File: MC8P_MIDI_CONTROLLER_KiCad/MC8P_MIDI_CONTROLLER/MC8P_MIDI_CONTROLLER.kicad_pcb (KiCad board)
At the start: 2 copper layers, 310.5 x 184.5 mm, 51 parts, among them J1 MIDI OUT, SW1 ASSIGN, SW2 ENTER, SW3 PREV, SW4 NEXT, U1 Teensy4.0

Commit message: V1.0.2
- KiCad Modifications
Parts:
- removed the G*** at (334.1, 61.6)
- added G***: LOGO, AXS_LOGO_KICAD:AXS_LOGO_FMASK_30X30, F.Cu at (224.5, 41.2)
- added G***: LOGO, MC8P_BITMAP_FOOTPRINTS:MC8P_MANUAL_QR_SLKSCR_20X20, F.Cu at (243.0, 39.5)
- added G***: LOGO, AXS_LOGO_KICAD:AXS_LOGO_FMASK_30X30, F.Cu at (78.5, 138.5)
- moved ? 7.00 mm to (324.5, 26.0)
- moved ? 7.00 mm to (324.5, 106.0)
- moved ? 7.00 mm to (181.5, 26.0)
- moved ? 7.00 mm to (169.0, 198.5)
- moved ? 7.00 mm to (181.5, 106.0)
- moved ? 7.00 mm to (26.0, 198.5)
- moved ? 7.00 mm to (26.0, 106.0)
- moved ? 7.00 mm to (169.0, 118.5)
- moved ? 7.00 mm to (26.0, 118.5)
- moved C1 7.00 mm to (76.0, 53.0)
- moved C2 7.00 mm to (81.0, 53.0)
- moved C3 7.00 mm to (86.0, 53.0)
- moved C4 7.00 mm to (91.0, 53.0)
- moved C5 7.00 mm to (111.0, 53.0)
- moved C6 7.00 mm to (106.0, 53.0)
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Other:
- board text added: ".AXS INTRUMENTS"
- board text added: "MAX"
- board text added: "MC8P"
- board text added: "MIN"
- board text added: "STANDALONE MIDI CONTROLLER"
- board text added: "TYPE A"

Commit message: v1.0.3
- Back panel finalised
- Exported gerbers
- Panelised for DIY kits
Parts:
- added G*** (x2): LOGO, MC8P_BITMAP_FOOTPRINTS:MC8P_PXLART_SPACE_FMASK_45X40, F.Cu at (251.9, 132.0)
- added G***: LOGO, MC8P_BITMAP_FOOTPRINTS:MC8P_PXLART_SPACE_FMASK_45X40, F.Cu at (256.2, 122.5)
- moved ? 162.1 mm to (271.0, 179.0), turned to 90 degrees
- moved ? 152.2 mm to (191.0, 179.0), turned to 90 degrees
- moved ? 90.1 mm to (271.0, 36.0), turned to 90 degrees
- moved ? 70.6 mm to (191.0, 36.0), turned to 90 degrees
- moved G*** 59.8 mm to (257.5, 97.5), turned to -90 degrees
- moved G*** 50.5 mm to (255.8, 80.8), turned to -90 degrees
- moved C1 14.1 mm to (86.0, 63.0)
- moved C2 14.1 mm to (91.0, 63.0)
- moved C3 14.1 mm to (96.0, 63.0)
- moved C4 14.1 mm to (101.0, 63.0)
- moved C5 14.1 mm to (121.0, 63.0)
- moved C6 14.1 mm to (116.0, 63.0)
- moved C7 14.1 mm to (111.0, 63.0)
- moved C8 14.1 mm to (106.0, 63.0)
- moved J1 14.1 mm to (48.5, 36.5)
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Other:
- board size 310.5 x 184.5 mm -> 247 x 196 mm
- board text added: ".AXS INSTRUMENTS"
- board text added: ">> NEXT"
- board text added: "I hope this controller becomes a trusted companion in your creative workflow - always ready to shape your sounds and aid in bringing your ideas to life! - Joe <3"
- board text added: "SNo."
- board text added: "THANK YOU"
- board text removed: "NEXT >>"

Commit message: Gerber Edits
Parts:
- moved ? 187.9 mm to (310.2, 181.1), turned to -90 degrees
- moved ? 184.6 mm to (310.2, 38.1), turned to -90 degrees
- moved ? 184.2 mm to (218.2, 181.2), turned to 90 degrees
- moved ? 174.3 mm to (218.2, 38.2), turned to 90 degrees
- moved REF** 160.5 mm to (205.5, 170.2), turned to 90 degrees
- moved ? 150.7 mm to (230.2, 181.1), turned to -90 degrees
- moved ? 146.6 mm to (230.2, 38.1), turned to -90 degrees
- moved REF** 145.5 mm to (46.2, 181.2), turned to 90 degrees
- moved REF** 143.8 mm to (205.5, 147.2), turned to 90 degrees
- moved REF** 134.6 mm to (181.5, 170.2), turned to 90 degrees
- moved REF** 133.1 mm to (205.5, 124.2), turned to 90 degrees
- moved REF** 132.8 mm to (46.2, 38.2), turned to 90 degrees
- moved J1 132.2 mm to (46.7, 168.7), turned to -90 degrees
- moved REF** 129.9 mm to (205.5, 101.2), turned to 90 degrees
- moved R5 124.5 mm to (60.6, 173.7), turned to 180 degrees
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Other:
- board size 247 x 196 mm -> 288 x 155 mm

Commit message: v1.0.4
- Design update with new logo
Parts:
- removed the G*** at (245.4, 136.4)
- removed the G*** at (158.2, 128.6)
- added G***: LOGO, AXS_LOGO_KICAD:AXS_LOGO_FMASK_20X20, F.Cu at (78.5, 136.5)
- added G***: LOGO, AXS_LOGO_KICAD:AXS_LOGO_FMASK_43X43, F.Cu at (97.5, 262.0)
- moved ? 304.4 mm to (26.0, 290.0), turned to 180 degrees
- moved ? 288.8 mm to (169.0, 290.0), turned to 180 degrees
- moved ? 206.3 mm to (26.0, 210.0), turned to 180 degrees
- moved ? 193.0 mm to (26.0, 198.0), turned to 0 degrees
- moved G*** 192.2 mm to (122.0, 229.1), turned to 0 degrees (x2)
- moved G*** 187.6 mm to (87.5, 223.5), turned to 0 degrees
- moved G*** 185.7 mm to (112.5, 224.8), turned to 0 degrees
- moved ? 182.4 mm to (169.0, 210.0), turned to 180 degrees
- moved REF** 169.2 mm to (37.0, 185.2), turned to 0 degrees
- moved ? 167.3 mm to (169.0, 198.0), turned to 0 degrees
- moved REF** 156.5 mm to (26.0, 26.0), turned to 0 degrees
- moved REF** 150.4 mm to (60.0, 185.2), turned to 0 degrees
- moved REF** 144.8 mm to (37.0, 161.3), turned to 0 degrees
- moved J1 142.4 mm to (38.5, 26.5), turned to 180 degrees
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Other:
- board size 288 x 155 mm -> 155 x 288 mm

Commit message: v1.0.6
-Adjustments to Front Panel and button positions
- Beginning Blender Models
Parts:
- moved SW1 1.50 mm to (135.0, 65.9)
- moved SW2 1.50 mm to (155.2, 65.9)
- moved SW3 1.50 mm to (135.0, 85.9)
- moved SW4 1.50 mm to (155.2, 85.9)
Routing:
- net D5: track 274.6 -> 278.5 mm
- net Vcc: track 486.5 -> 489.9 mm
- net D7: track 254.8 -> 257.7 mm
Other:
- outline, holes or cut-outs redrawn

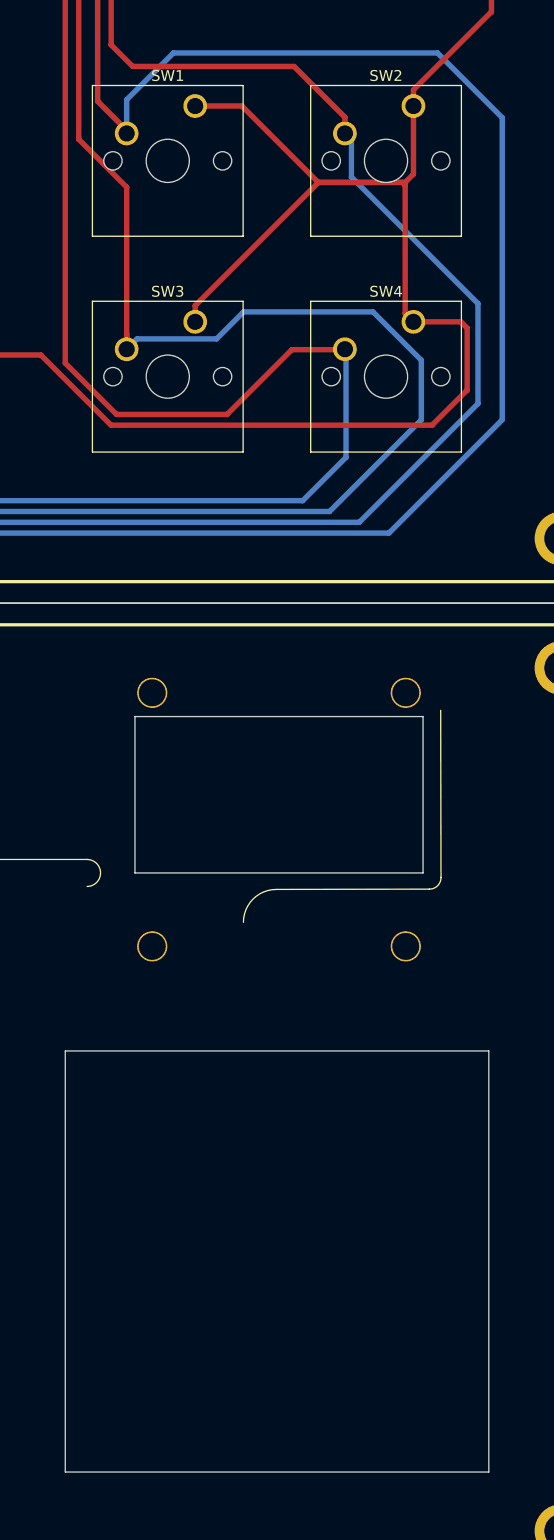
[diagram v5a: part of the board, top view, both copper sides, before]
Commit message: v1.0.9
- Panel alterations
- Sketchup alterations
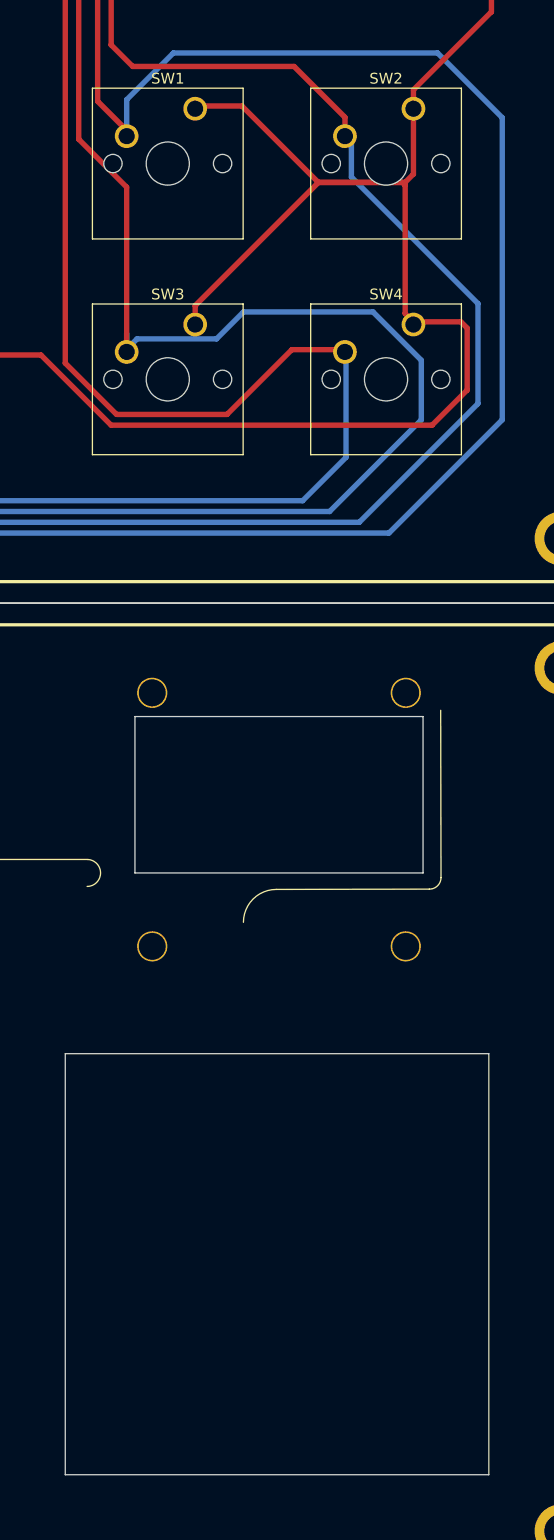
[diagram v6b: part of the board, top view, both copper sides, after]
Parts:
- moved SW1 0.25 mm to (135.0, 66.2)
- moved SW2 0.25 mm to (155.2, 66.2)
- moved SW3 0.25 mm to (135.0, 86.2)
- moved SW4 0.25 mm to (155.2, 86.2)
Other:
- outline, holes or cut-outs redrawn

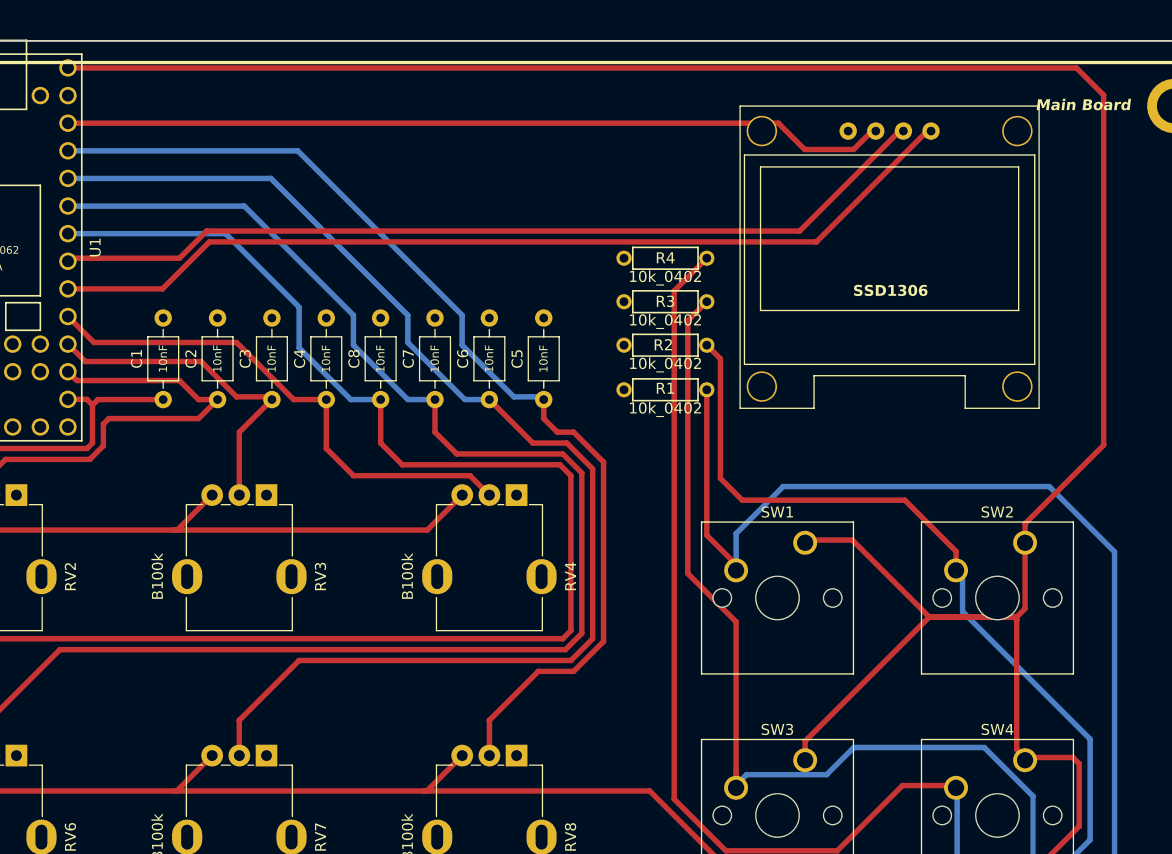
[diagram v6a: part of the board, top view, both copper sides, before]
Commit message: v1.1.0
- PCB Fixes
- firmware descriptor adjustments
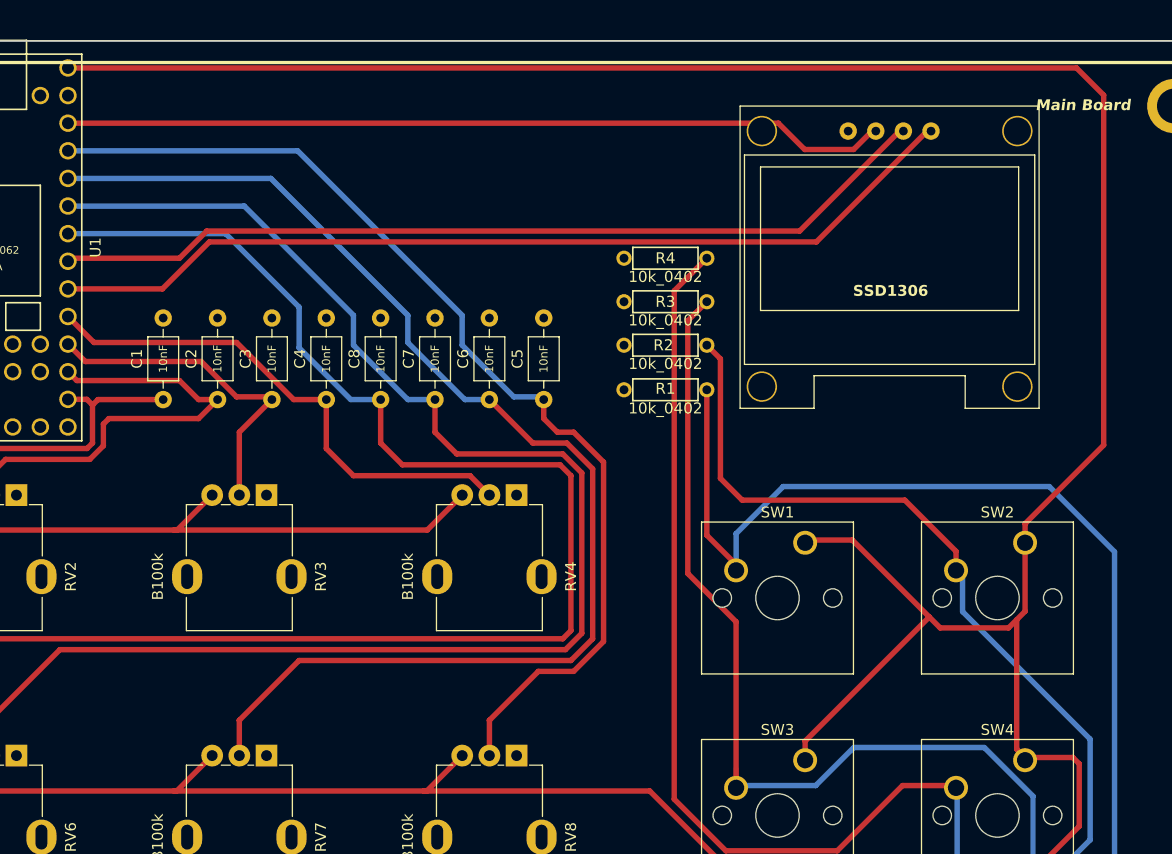
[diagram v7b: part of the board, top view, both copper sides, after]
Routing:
- net Vcc: track 489.9 -> 482.5 mm
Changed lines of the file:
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@@
 			(drillshape 0)
 			(scaleselection 1)
-			(outputdirectory "MC8P_MIDI_CONTROLLER_GBRS/")
+			(outputdirectory "MC8P_MIDI_CONTROLLER_GBRS/MC8P_MAINBOARD_GBRS/")
 		)
 	)
@@
 	)
 	(segment
-		(start 155.98 89.48)
-		(end 151.5 85)
+		(start 47.73 44.75)
+		(end 47.73 99.25)
 		(width 0.5)
 		(layer "B.Cu")
@@
 	)
 	(segment
-		(start 129.63 87.5)
-		(end 128.67 88.46)
+		(start 49.66 42.82)
+		(end 47.73 44.75)
 		(width 0.5)
 		(layer "B.Cu")
@@
 	)
 	(segment
-		(start 47.73 99.25)
-		(end 51.98 103.5)
+		(start 151.5 85)
+		(end 139.5 85)
 		(width 0.5)
 		(layer "B.Cu")
@@
 	)
 	(segment
-		(start 137 87.5)
-		(end 129.63 87.5)
+		(start 155.98 89.48)
+		(end 151.5 85)
 		(width 0.5)
 		(layer "B.Cu")
@@
 	)
 	(segment
-		(start 51.98 103.5)
-		(end 147.48 103.5)
+		(start 47.73 99.25)
+		(end 51.98 103.5)
 		(width 0.5)
 		(layer "B.Cu")
@@
 	)
 	(segment
-		(start 139.5 85)
-		(end 137 87.5)
+		(start 147.48 103.5)
+		(end 155.98 95)
 		(width 0.5)
 		(layer "B.Cu")
@@
 	)
 	(segment
-		(start 47.73 44.75)
-		(end 47.73 99.25)
+		(start 155.98 95)
+		(end 155.98 89.48)
 		(width 0.5)
 		(layer "B.Cu")
@@
 	)
 	(segment
-		(start 128.67 88.46)
-		(end 128.67 86.96)
+		(start 51.98 103.5)
+		(end 147.48 103.5)
 		(width 0.5)
 		(layer "B.Cu")
@@
 	)
 	(segment
-		(start 155.98 95)
-		(end 155.98 89.48)
+		(start 136 88.5)
+		(end 128.71 88.5)
 		(width 0.5)
 		(layer "B.Cu")
@@
 	)
 	(segment
-		(start 151.5 85)
-		(end 139.5 85)
+		(start 128.71 88.5)
+		(end 128.67 88.46)
 		(width 0.5)
 		(layer "B.Cu")
@@
 	)
 	(segment
-		(start 49.66 42.82)
-		(end 47.73 44.75)
+		(start 128.67 88.46)
+		(end 128.67 86.96)
 		(width 0.5)
 		(layer "B.Cu")
@@
 	)
 	(segment
-		(start 147.48 103.5)
-		(end 155.98 95)
+		(start 51.98 42.82)
+		(end 49.66 42.82)
 		(width 0.5)
 		(layer "B.Cu")
@@
 	)
 	(segment
-		(start 51.98 42.82)
-		(end 49.66 42.82)
+		(start 139.5 85)
+		(end 136 88.5)
 		(width 0.5)
 		(layer "B.Cu")
@@
 	)
 	(segment
-		(start 154.48 73)
-		(end 155.25 72.23)
-		(width 0.5)
-		(layer "F.Cu")
-		(net 14)
-	)
-	(segment
 		(start 80.4827 61.7842)
 		(end 77.2669 65)
@@
 	)
 	(segment
+		(start 154.48 73.25)
+		(end 155.25 72.48)
+		(width 0.5)
+		(layer "F.Cu")
+		(net 14)
+	)
+	(segment
+		(start 159.98 22.5)
+		(end 67.22 22.5)
+		(width 0.5)
+		(layer "F.Cu")
+		(net 14)
+	)
+	(segment
 		(start 156.98 95.5)
 		(end 127.23 95.5)
@@
 	)
 	(segment
-		(start 34.4827 67.4973)
-		(end 34.4827 85.7442)
+		(start 147.44 74)
+		(end 153.73 74)
 		(width 0.5)
 		(layer "F.Cu")
@@
 	)
 	(segment
-		(start 155.25 85.92)
-		(end 159.65 85.92)
-		(width 0.5)
-		(layer "F.Cu")
-		(net 14)
-	)
-	(segment
-		(start 154.23 73)
-		(end 154.48 73.25)
+		(start 34.4827 67.4973)
+		(end 34.4827 85.7442)
 		(width 0.5)
 		(layer "F.Cu")
@@
 	)
 	(segment
-		(start 67.22 22.5)
-		(end 159.98 22.5)
+		(start 155.25 85.92)
+		(end 159.65 85.92)
 		(width 0.5)
 		(layer "F.Cu")
@@
 	)
 	(segment
-		(start 146.44 73)
-		(end 154.48 73)
-		(width 0.5)
-		(layer "F.Cu")
-		(net 14)
-	)
-	(segment
-		(start 155.25 72.23)
-		(end 155.25 64.42)
-		(width 0.5)
-		(layer "F.Cu")
-		(net 14)
-	)
-	(segment
 		(start 34.4827 86.5027)
 		(end 36.98 89)
@@
 	)
 	(segment
-		(start 162.48 57.19)
-		(end 155.25 64.42)
+		(start 36.98 65)
+		(end 54.98 65)
 		(width 0.5)
 		(layer "F.Cu")
@@
 	)
 	(segment
-		(start 36.98 65)
-		(end 54.98 65)
+		(start 34.4827 50.1173)
+		(end 40.98 43.62)
 		(width 0.5)
 		(layer "F.Cu")
@@
 	)
 	(segment
-		(start 34.4827 50.1173)
-		(end 40.98 43.62)
+		(start 162.48 57.19)
+		(end 162.48 25)
 		(width 0.5)
 		(layer "F.Cu")
@@
 	)
 	(segment
+		(start 146.44 73)
+		(end 147.44 74)
+		(width 0.5)
+		(layer "F.Cu")
+		(net 14)
+	)
+	(segment
 		(start 34.4827 61.7842)
 		(end 34.4827 50.1173)
@@
 	)
 	(segment
-		(start 154.48 73)
-		(end 154.48 73.25)
+		(start 155.25 64.42)
+		(end 162.48 57.19)
 		(width 0.5)
 		(layer "F.Cu")
@@
 	)
 	(segment
-		(start 146.44 73)
-		(end 154.23 73)
-		(width 0.5)
-		(layer "F.Cu")
-		(net 14)
-	)
-	(segment
 		(start 53.98 89)
 		(end 76.98 89)
@@
 	)
 	(segment
-		(start 76.98 89)
-		(end 99.98 89)
+		(start 153.73 74)
+		(end 154.48 73.25)
 		(width 0.5)
 		(layer "F.Cu")
@@
 	)
 	(segment
-		(start 162.48 25)
-		(end 162.48 57.19)
+		(start 155.25 72.48)
+		(end 155.25 64.42)
 		(width 0.5)
 		(layer "F.Cu")
@@
 	)
 	(segment
-		(start 127.23 95.5)
-		(end 120.73 89)
+		(start 76.98 89)
+		(end 99.98 89)
 		(width 0.5)
 		(layer "F.Cu")
@@
 	)
 	(segment
-		(start 159.98 22.5)
-		(end 162.48 25)
+		(start 162.48 25)
+		(end 159.98 22.5)
+		(width 0.5)
+		(layer "F.Cu")
+		(net 14)
+	)
+	(segment
+		(start 127.23 95.5)
+		(end 120.73 89)
 		(width 0.5)
 		(layer "F.Cu")

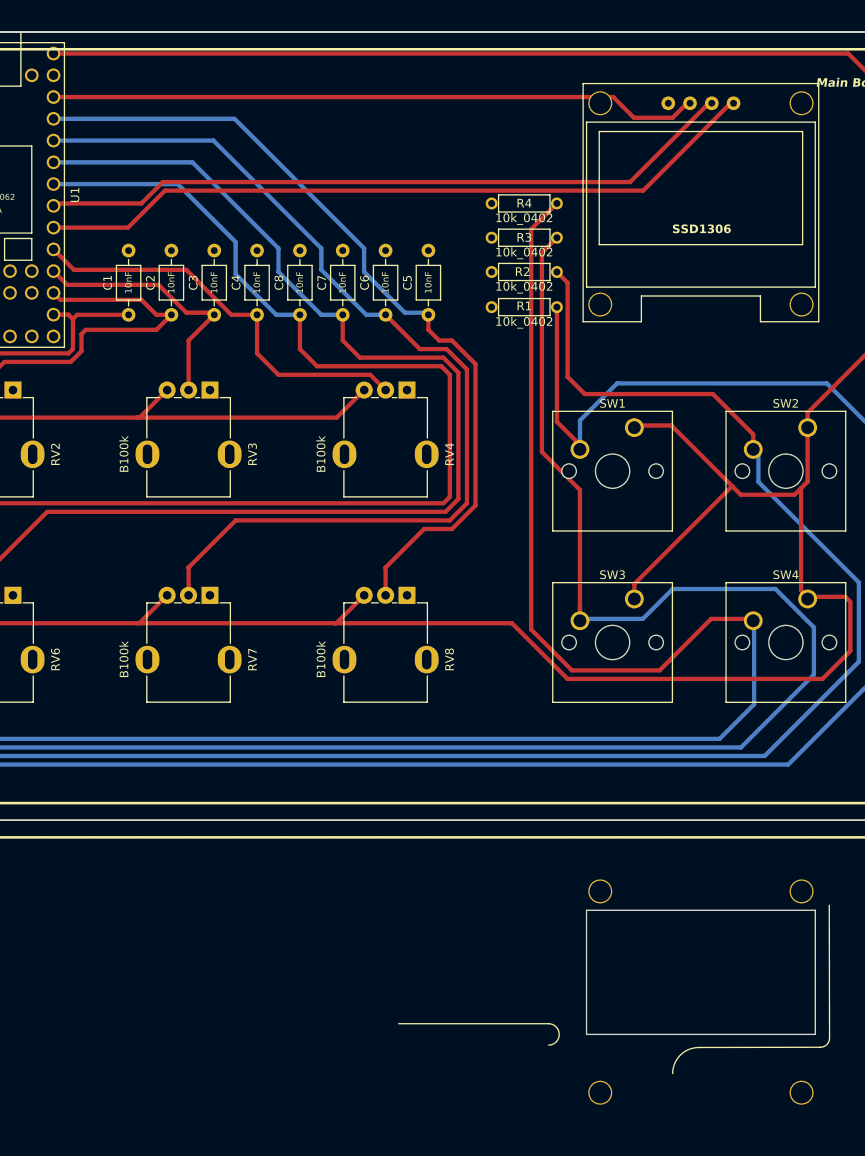
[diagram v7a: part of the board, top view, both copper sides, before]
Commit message: Power stability
- Added capacitors to add power stability
- Adjusted Front panel + gerbers
- Adjusted Main Board + gerbers
- Re-frabricated panel gerbers
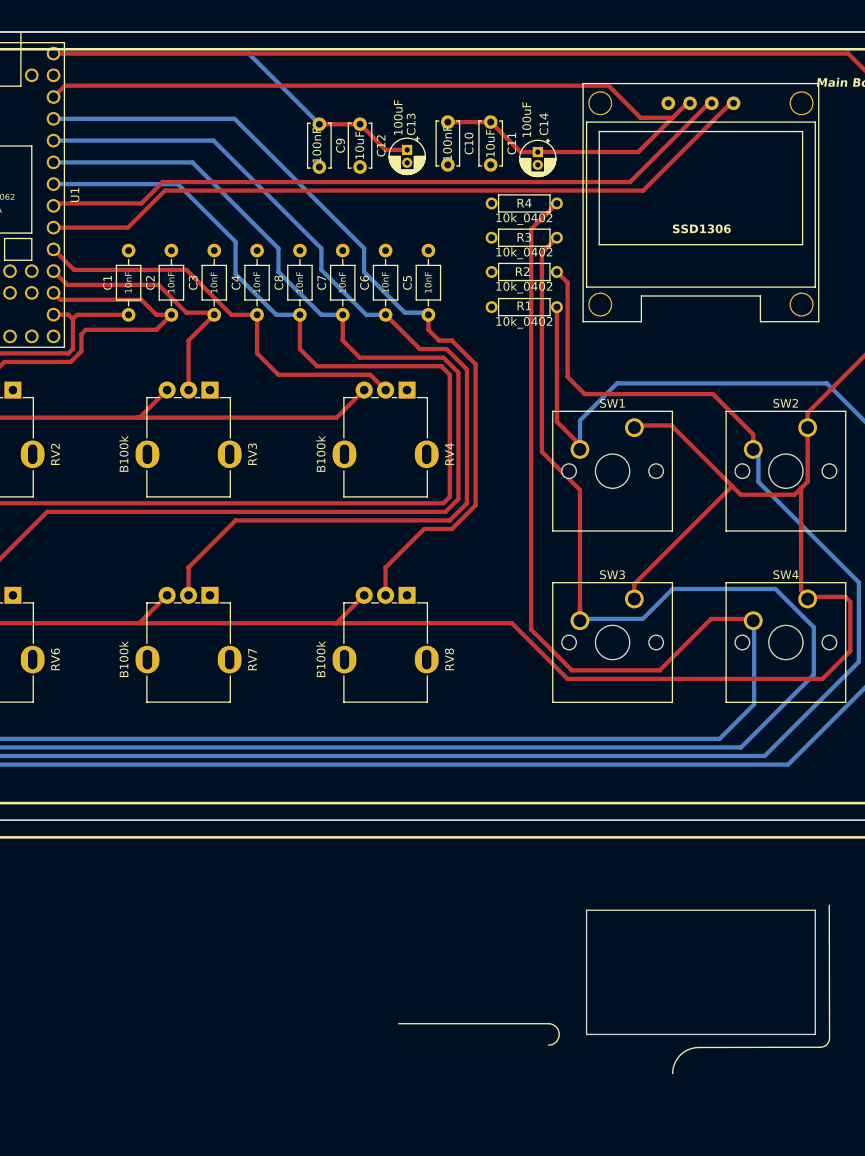
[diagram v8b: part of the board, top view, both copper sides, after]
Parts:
- removed the SSD1306 at (156.5, 145.8)
- added C10: 100nF, Capacitor_THT:C_Disc_D5.0mm_W2.5mm_P5.00mm, F.Cu at (113.2, 30.5)
- added C11: 10uF, Capacitor_THT:C_Disc_D5.0mm_W2.5mm_P5.00mm, F.Cu at (118.2, 30.5)
- added C12: 10uF, Capacitor_THT:C_Disc_D5.0mm_W2.5mm_P5.00mm, F.Cu at (103.0, 30.8)
- added C13: 100uF, Capacitor_THT:CP_Radial_D4.0mm_P1.50mm, F.Cu at (108.5, 33.8)
- added C14: 100uF, Capacitor_THT:CP_Radial_D4.0mm_P1.50mm, F.Cu at (123.8, 34.0)
- added C9: 100nF, Capacitor_THT:C_Disc_D5.0mm_W2.5mm_P5.00mm, F.Cu at (98.2, 30.8)
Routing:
- net Vcc: track 482.5 -> 528.5 mm
- net 3V3: track 76.1 -> 106.5 mm
